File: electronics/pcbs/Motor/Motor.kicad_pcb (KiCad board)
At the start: 2 copper layers, 101.6 x 53.3 mm, 17 parts, among them J1 Left Encoder, J2 Right Encoder, J3 Battery, J4 I2C, P1 Digital, P10 CONN_01X01, P11 CONN_01X01, P12 CONN_01X01, P13 CONN_01X01, P2 Power, P3 Analog, P4 Analog, P5 PWM, P6 PWM, P7 Communication, P8 CONN_01X01, P9 CONN_01X01

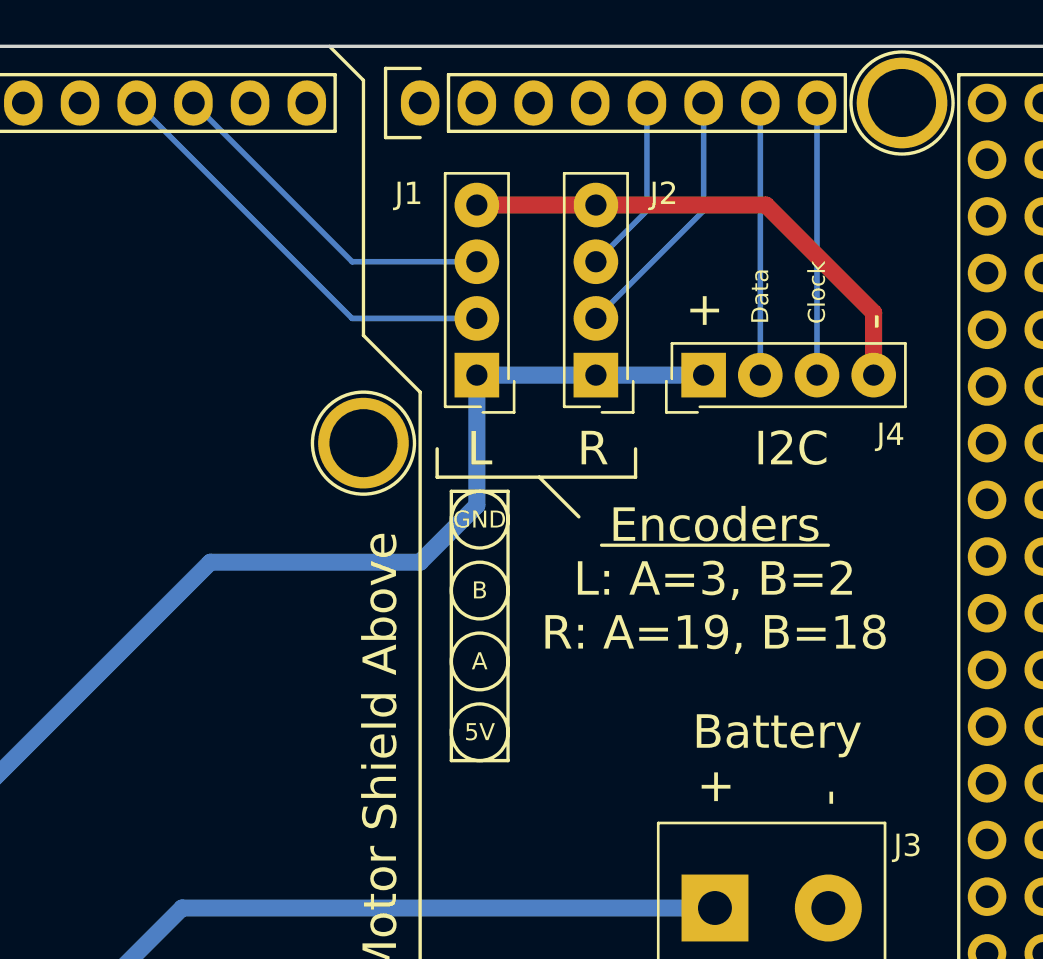
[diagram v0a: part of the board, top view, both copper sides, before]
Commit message: Primary/Motor PCBs: Rearranged the GND pin on breakout headers so that we can avoid needing two layers. This change makes the boards more easily prototyped using hobbyist tools like the OtherMill, where plating holes and vias is difficult.
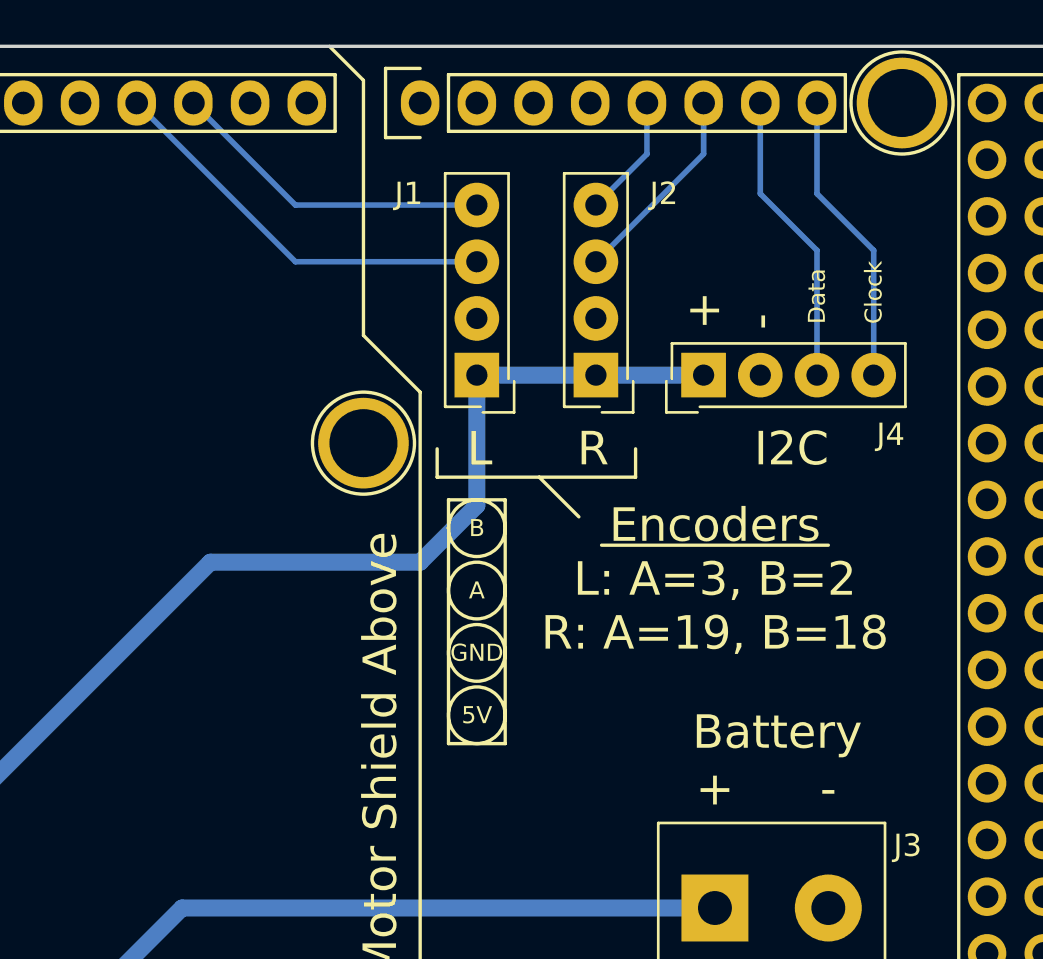
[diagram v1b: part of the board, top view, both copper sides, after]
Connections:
- J1 pad 2: /3(**) -> GND
- J1 pad 3: /2(**) -> /3(**)
- J1 pad 4: GND -> /2(**)
- J2 pad 2: /19(Rx1) -> GND
- J2 pad 3: /18(Tx1) -> /19(Rx1)
- J2 pad 4: GND -> /18(Tx1)
- J4 pad 2: /20(SDA) -> GND
- J4 pad 3: /21(SCL) -> /20(SDA)
- J4 pad 4: GND -> /21(SCL)
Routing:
- net GND: track 22.6 -> 0.00 mm
- net /19(Rx1): track 11.7 -> 9.11 mm
- net /18(Tx1): track 8.06 -> 5.52 mm
- net /3(**): track 19.2 -> 18.2 mm
- net /21(SCL): track 12.2 -> 13.2 mm
- net /20(SDA): track 12.2 -> 13.2 mm
- net /2(**): track 15.6 -> 14.6 mm

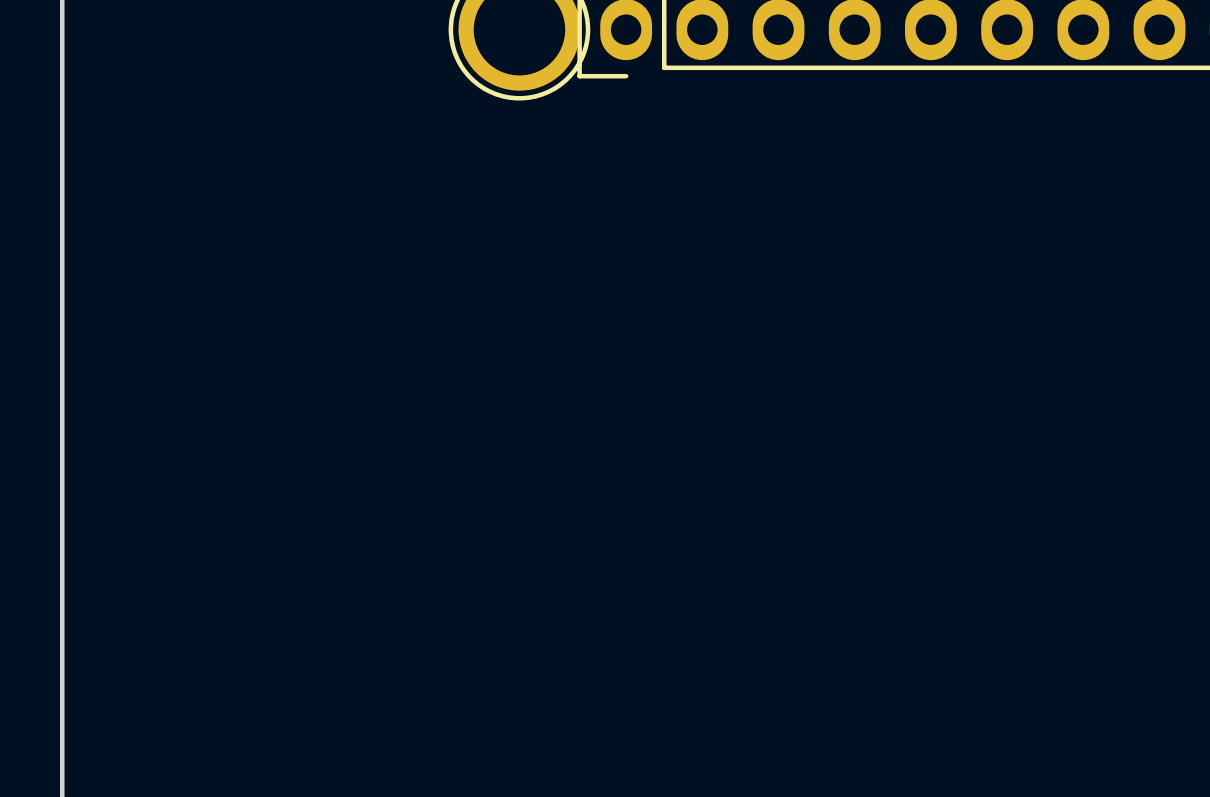
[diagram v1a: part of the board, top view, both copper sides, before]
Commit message: Primary/Motor PCBs: Added logo and competition to board silkscreens.
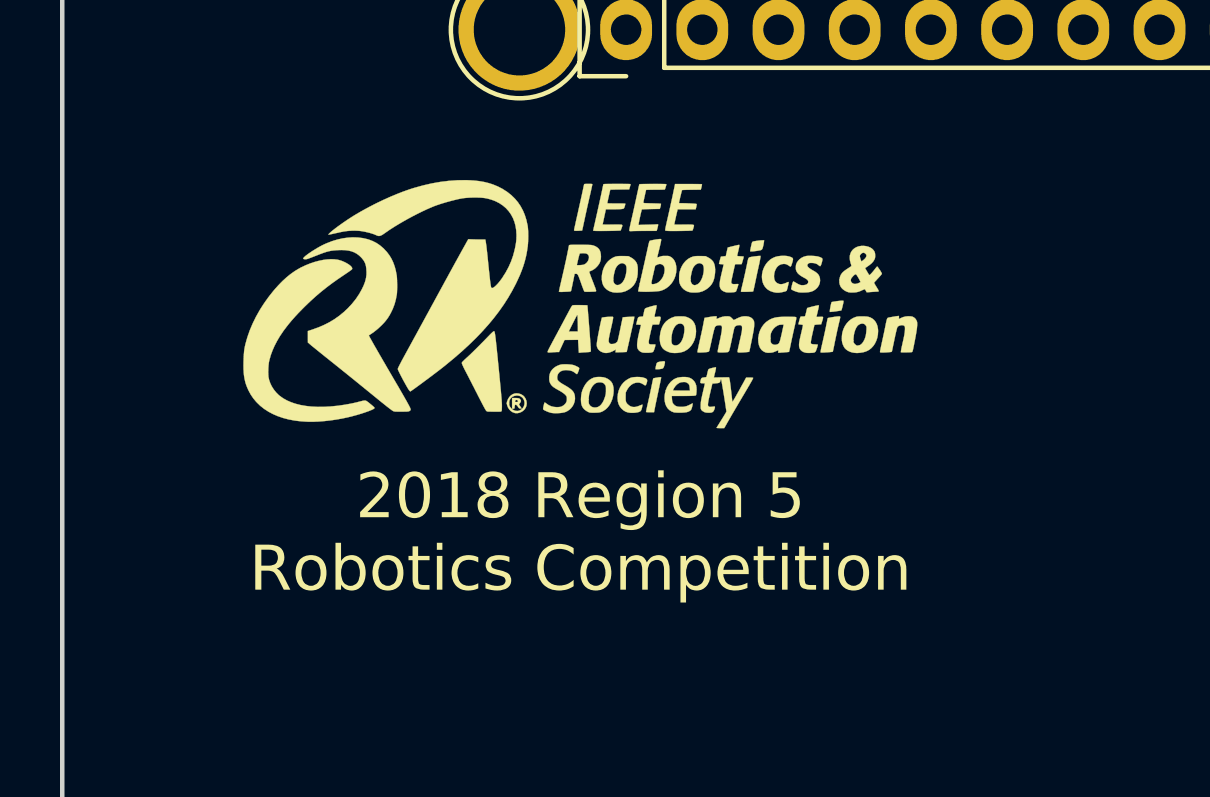
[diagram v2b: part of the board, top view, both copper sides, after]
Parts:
- added G***: LOGO, RAS:Logo, F.Cu at (120.7, 80.0)
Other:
- board text added: "2018 Region 5 Robotics Competition"

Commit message: merge issues
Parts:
- removed P8: CONN_01X01, Socket_Arduino_Mega:Arduino_1pin
- moved G*** 12.7 mm to (133.3, 80.0)
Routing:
- added copper zone on F.Cu, net GND
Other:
- board size 101.6 x 53.3 mm -> 86.5 x 53.3 mm
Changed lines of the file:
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@@
 (kicad_pcb (version 4) (host pcbnew 4.0.7)
   (general
-    (links 26)
+    (links 25)
     (no_connects 2)
-    (area 96.952999 66.843 205.053001 122.995)
+    (area 96.952999 66.843 204.931334 122.995)
     (thickness 1.6)
-    (drawings 69)
+    (drawings 89)
     (tracks 23)
     (zones 0)
-    (modules 18)
+    (modules 17)
     (nets 81)
   )
@@
     (35 F.Paste user)
     (36 B.SilkS user)
-    (37 F.SilkS user)
+    (37 F.SilkS user hide)
     (38 B.Mask user)
     (39 F.Mask user)
@@
     (45 Margin user)
     (46 B.CrtYd user)
-    (47 F.CrtYd user)
+    (47 F.CrtYd user hide)
     (48 B.Fab user)
     (49 F.Fab user hide)
@@
     (zone_45_only no)
     (trace_min 0.2)
-    (segment_width 0.15)
-    (edge_width 0.15)
+    (segment_width 0.4064)
+    (edge_width 0.4064)
     (via_size 0.6)
     (via_drill 0.4)
@@
     (pad_drill 3.048)
     (pad_to_mask_clearance 0)
-    (aux_axis_origin 103.378 121.666)
+    (aux_axis_origin 116.078 121.666)
+    (grid_origin 116.078 121.666)
     (visible_elements 7FFEFF7F)
     (pcbplotparams
@@
   )
   (module Socket_Arduino_Mega:Arduino_1pin locked (layer F.Cu)
-    (at 117.348 119.126)
-    (descr "module 1 pin (ou trou mecanique de percage)")
-    (tags DEV)
-    (fp_text reference P8 (at 0 -3.048) (layer F.SilkS) hide
-      (effects (font (size 1 1) (thickness 0.15)))
-    )
-    (fp_text value CONN_01X01 (at 0 2.794) (layer F.Fab) hide
-      (effects (font (size 1 1) (thickness 0.15)))
-    )
-    (fp_circle (center 0 0) (end 0 -2.286) (layer F.SilkS) (width 0.15))
-    (pad 1 thru_hole circle (at 0 0) (size 4.064 4.064) (drill 3.048) (layers *.Cu *.Mask F.SilkS)
-      (net 1 GND))
-  )
-  (module Socket_Arduino_Mega:Arduino_1pin locked (layer F.Cu)
     (at 169.418 114.046)
     (descr "module 1 pin (ou trou mecanique de percage)")
@@
   )
   (module RAS:Logo (layer F.Cu)
-    (at 120.65 80.01)
+    (at 133.35 80.01)
     (fp_text reference G*** (at 0 0) (layer F.SilkS) hide
       (effects (font (thickness 0.3)))
@@
       (xy -2.277533 3.132666) (xy -2.182283 3.132713)) (layer F.SilkS) (width 0.01))
   )
-  (gr_text "2018 Region 5\nRobotics Competition" (at 120.65 87.63) (layer F.SilkS)
+  (gr_line (start 173.228 99.822) (end 173.228 88.138) (angle 90) (layer Cmts.User) (width 0.4064))
+  (gr_line (start 175.768 99.822) (end 173.228 99.822) (angle 90) (layer Cmts.User) (width 0.4064))
+  (gr_line (start 175.768 88.138) (end 175.768 99.822) (angle 90) (layer Cmts.User) (width 0.4064))
+  (gr_line (start 173.228 88.138) (end 175.768 88.138) (angle 90) (layer Cmts.User) (width 0.4064))
+  (gr_text - (at 190.246 101.6) (layer F.SilkS)
+    (effects (font (size 1.5 1.5) (thickness 0.3)))
+  )
+  (gr_text + (at 185.166 101.6) (layer Cmts.User)
+    (effects (font (size 1.651 1.651) (thickness 0.4064)))
+  )
+  (gr_text Battery (at 187.96 99.06) (layer Cmts.User)
+    (effects (font (size 1.651 1.651) (thickness 0.4064)))
+  )
+  (gr_text Clock (at 192.278 80.772 90) (layer Cmts.User)
+    (effects (font (size 1.651 1.651) (thickness 0.4064)) (justify left))
+  )
+  (gr_text Data (at 189.738 80.772 90) (layer Cmts.User)
+    (effects (font (size 1.651 1.651) (thickness 0.4064)) (justify left))
+  )
+  (gr_text - (at 187.198 81.026 90) (layer Cmts.User)
+    (effects (font (size 1.651 1.651) (thickness 0.4064)) (justify left))
+  )
+  (gr_text + (at 184.658 81.026 90) (layer Cmts.User)
+    (effects (font (size 1.651 1.651) (thickness 0.4064)) (justify left))
+  )
+  (gr_text I2C (at 188.722 86.36) (layer Cmts.User)
+    (effects (font (size 1.651 1.651) (thickness 0.4064)))
+  )
+  (gr_text "Encoders\nL: A=3, B=2\nR: A=19, B=18" (at 185.928 92.202) (layer Cmts.User)
+    (effects (font (size 1.651 1.651) (thickness 0.4064)))
+  )
+  (gr_line (start 169.418 69.85) (end 167.894 68.326) (angle 90) (layer Cmts.User) (width 0.4064))
+  (gr_line (start 169.418 81.28) (end 169.418 69.85) (angle 90) (layer Cmts.User) (width 0.4064))
+  (gr_line (start 171.958 83.82) (end 169.418 81.28) (angle 90) (layer Cmts.User) (width 0.4064))
+  (gr_line (start 171.958 116.586) (end 171.958 83.82) (angle 90) (layer Cmts.User) (width 0.4064))
+  (gr_text "Motor Shield\nAbove" (at 168.91 99.568 90) (layer Cmts.User)
+    (effects (font (size 1.651 1.651) (thickness 0.4064)))
+  )
+  (gr_text + (at 174.498 98.298) (layer Cmts.User)
+    (effects (font (size 1.651 1.651) (thickness 0.4064)))
+  )
+  (gr_text - (at 174.498 95.504) (layer Cmts.User)
+    (effects (font (size 1.651 1.651) (thickness 0.4064)))
+  )
+  (gr_text A (at 174.498 92.71) (layer Cmts.User)
+    (effects (font (size 1.651 1.651) (thickness 0.4064)))
+  )
+  (gr_text B (at 174.498 89.916) (layer F.SilkS)
+    (effects (font (size 0.762 0.762) (thickness 0.1905)))
+  )
+  (gr_text R (at 179.832 86.106) (layer F.SilkS)
+    (effects (font (size 1.5 1.5) (thickness 0.3)))
+  )
+  (gr_text L (at 174.498 86.106) (layer F.SilkS)
+    (effects (font (size 1.5 1.5) (thickness 0.3)))
+  )
+  (gr_text "2018 Region 5\nRobotics Competition" (at 133.985 87.63) (layer Cmts.User)
+    (effects (font (size 1.651 1.651) (thickness 0.4064)))
+  )
+  (gr_line (start 202.565 68.326) (end 202.565 121.666) (angle 90) (layer Edge.Cuts) (width 0.4064))
+  (gr_text "2018 Region 5\nRobotics Competition" (at 133.985 87.63) (layer F.SilkS)
     (effects (font (size 1.5 1.5) (thickness 0.3)))
   )
@@
     (effects (font (size 1.5 1.5) (thickness 0.3)))
   )
-  (gr_text - (at 190.246 101.6) (layer F.SilkS)
-    (effects (font (size 1.5 1.5) (thickness 0.3)))
+  (gr_text - (at 190.246 101.6) (layer Cmts.User)
+    (effects (font (size 1.651 1.651) (thickness 0.4064)))
   )
   (gr_text + (at 185.166 101.6) (layer F.SilkS)
@@
     (effects (font (size 1.5 1.5) (thickness 0.3)))
   )
-  (gr_text R (at 179.705 86.36) (layer F.SilkS)
-    (effects (font (size 1.5 1.5) (thickness 0.3)))
-  )
-  (gr_text L (at 174.625 86.36) (layer F.SilkS)
-    (effects (font (size 1.5 1.5) (thickness 0.3)))
+  (gr_text R (at 179.832 86.106) (layer Cmts.User)
+    (effects (font (size 1.651 1.651) (thickness 0.4064)))
+  )
+  (gr_text L (at 174.498 86.106) (layer Cmts.User)
+    (effects (font (size 1.651 1.651) (thickness 0.4064)))
   )
   (gr_line (start 181.61 87.63) (end 181.61 86.36) (angle 90) (layer F.SilkS) (width 0.15))
@@
     (effects (font (size 0.762 0.762) (thickness 0.1905)))
   )
-  (gr_text B (at 174.498 89.916) (layer F.SilkS)
-    (effects (font (size 0.762 0.762) (thickness 0.1905)))
+  (gr_text B (at 174.498 89.916) (layer Cmts.User)
+    (effects (font (size 1.651 1.651) (thickness 0.4064)))
   )
   (gr_text GND (at 174.498 95.504) (layer F.SilkS)
@@
   (gr_line (start 114.808 109.601) (end 114.808 118.491) (angle 90) (layer Dwgs.User) (width 0.15))
   (gr_line (start 101.473 109.601) (end 114.808 109.601) (angle 90) (layer Dwgs.User) (width 0.15))
-  (gr_line (start 202.438 121.666) (end 103.378 121.666) (angle 90) (layer Edge.Cuts) (width 0.15))
-  (gr_line (start 202.438 120.396) (end 202.438 121.666) (angle 90) (layer Edge.Cuts) (width 0.15))
-  (gr_line (start 204.978 117.856) (end 202.438 120.396) (angle 90) (layer Edge.Cuts) (width 0.15))
-  (gr_line (start 204.978 83.566) (end 204.978 117.856) (angle 90) (layer Edge.Cuts) (width 0.15))
-  (gr_line (start 202.438 81.026) (end 204.978 83.566) (angle 90) (layer Edge.Cuts) (width 0.15))
-  (gr_line (start 202.438 70.866) (end 202.438 81.026) (angle 90) (layer Edge.Cuts) (width 0.15))
-  (gr_line (start 199.898 68.326) (end 202.438 70.866) (angle 90) (layer Edge.Cuts) (width 0.15))
-  (gr_line (start 103.378 68.326) (end 199.898 68.326) (angle 90) (layer Edge.Cuts) (width 0.15))
-  (gr_line (start 103.378 121.666) (end 103.378 68.326) (angle 90) (layer Edge.Cuts) (width 0.15))
+  (gr_line (start 202.565 121.666) (end 116.078 121.666) (angle 90) (layer Edge.Cuts) (width 0.4064))
+  (gr_line (start 116.078 68.326) (end 202.565 68.326) (angle 90) (layer Edge.Cuts) (width 0.4064))
+  (gr_line (start 116.078 121.666) (end 116.078 68.326) (angle 90) (layer Edge.Cuts) (width 0.4064))
   (segment (start 174.498 83.058) (end 174.498 88.9) (width 0.762) (layer B.Cu) (net 34))
   (segment (start 141.478 112.522) (end 141.478 119.126) (width 0.762) (layer B.Cu) (net 34))
@@
     (connect_pads (clearance 0.508))
     (min_thickness 0.254)
-    (fill yes (arc_segments 16) (thermal_gap 1.016) (thermal_bridge_width 0.762))
+    (fill yes (arc_segments 16) (thermal_gap 0.508) (thermal_bridge_width 0.508))
     (polygon
       (pts
-        (xy 202.438 70.866) (xy 202.438 81.026) (xy 204.978 83.566) (xy 204.978 117.856) (xy 202.438 120.396)
-        (xy 202.438 121.666) (xy 103.378 121.666) (xy 103.378 68.326) (xy 199.898 68.326)
+        (xy 202.565 121.666) (xy 116.078 121.666) (xy 116.078 68.326) (xy 202.565 68.326)
       )
     )
+  )
+  (zone (net 1) (net_name GND) (layer F.Cu) (hatch edge 0.508)
+    (connect_pads (clearance 0.508))
+    (min_thickness 0.254)
+    (fill yes (arc_segments 16) (thermal_gap 0.508) (thermal_bridge_width 0.508))
+    (polygon
+      (pts
+        (xy 202.565 121.666) (xy 116.078 121.666) (xy 116.078 68.326) (xy 202.565 68.326)
+      )
+    )
